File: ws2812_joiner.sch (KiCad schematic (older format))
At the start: 22 parts, among them P1 CONN_01X03, P10 CONN_01X03, P2 CONN_01X03, P3 CONN_01X03, P4 CONN_01X03, P5 CONN_01X03, P6 CONN_01X03, P7 CONN_01X03, P8 CONN_01X03, P9 CONN_01X03

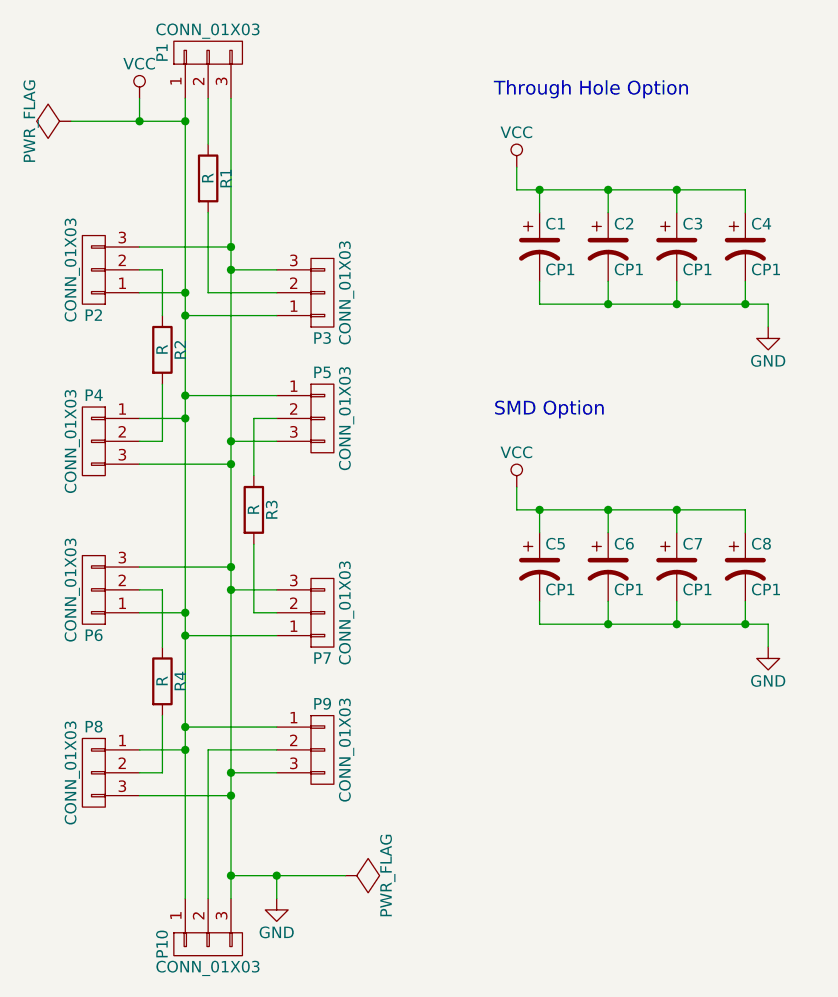
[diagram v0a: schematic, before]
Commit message: Version 2 - use SMD tantalum caps to neaten everything up. Duplicate silkscreen graphics to the front where possible and add component values.
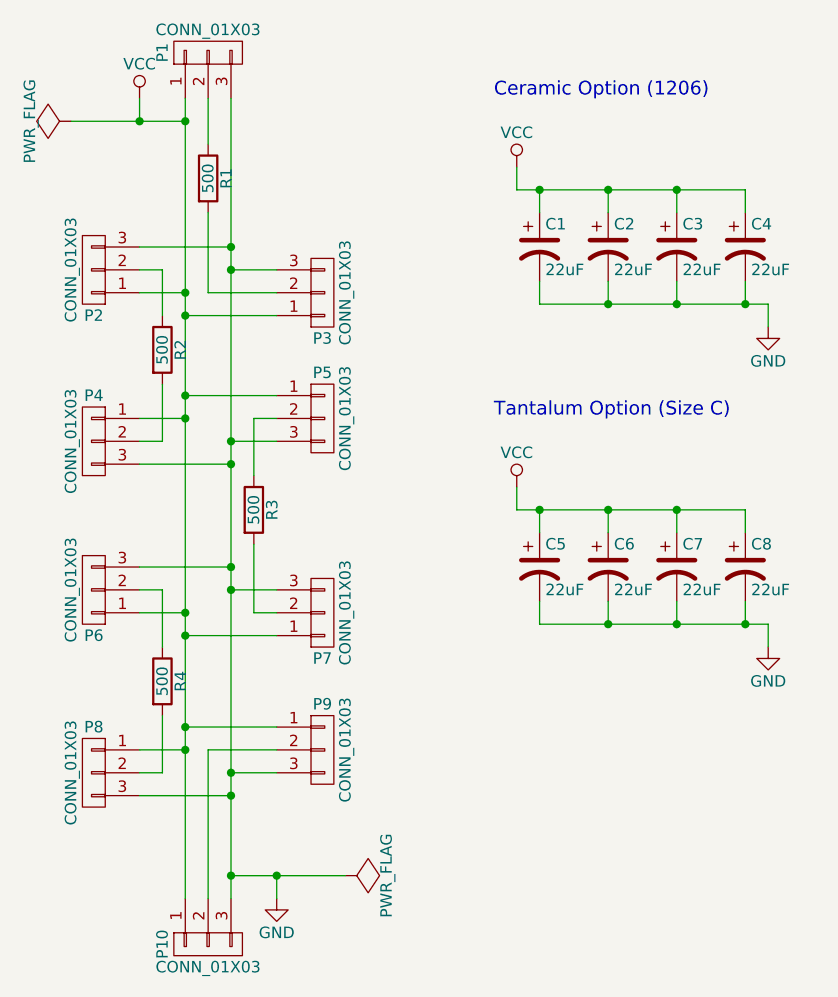
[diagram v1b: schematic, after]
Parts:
- C1, C2, C3, C4: value CP1 -> 22uF; footprint Capacitors_ThroughHole:CP_Radial_D10.0mm_P2.50mm_P5.00mm -> Capacitors_Tantalum_SMD:CP_Tantalum_Case-C_EIA-6032-28_Reflow
- C5, C6, C7, C8: value CP1 -> 22uF
- R1, R2, R3, R4: value R -> 500
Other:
- note added: "Ceramic Option (1206)"
- note added: "Tantalum Option (Size C)"
- note removed: "SMD Option"
- note removed: "Through Hole Option"
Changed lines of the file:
@@
 P 7200 2700
 F 0 "C1" H 7225 2800 50  0000 L CNN
-F 1 "CP1" H 7225 2600 50  0000 L CNN
-F 2 "Capacitors_ThroughHole:CP_Radial_D10.0mm_P2.50mm_P5.00mm" H 7200 2700 50  0001 C CNN
+F 1 "22uF" H 7225 2600 50  0000 L CNN
+F 2 "Capacitors_Tantalum_SMD:CP_Tantalum_Case-C_EIA-6032-28_Reflow" H 7200 2700 50  0001 C CNN
 F 3 "" H 7200 2700 50  0000 C CNN
 	1    7200 2700
@@
 P 7500 2700
 F 0 "C2" H 7525 2800 50  0000 L CNN
-F 1 "CP1" H 7525 2600 50  0000 L CNN
-F 2 "Capacitors_ThroughHole:CP_Radial_D10.0mm_P2.50mm_P5.00mm" H 7500 2700 50  0001 C CNN
+F 1 "22uF" H 7525 2600 50  0000 L CNN
+F 2 "Capacitors_Tantalum_SMD:CP_Tantalum_Case-C_EIA-6032-28_Reflow" H 7500 2700 50  0001 C CNN
 F 3 "" H 7500 2700 50  0000 C CNN
 	1    7500 2700
@@
 P 7800 2700
 F 0 "C3" H 7825 2800 50  0000 L CNN
-F 1 "CP1" H 7825 2600 50  0000 L CNN
-F 2 "Capacitors_ThroughHole:CP_Radial_D10.0mm_P2.50mm_P5.00mm" H 7800 2700 50  0001 C CNN
+F 1 "22uF" H 7825 2600 50  0000 L CNN
+F 2 "Capacitors_Tantalum_SMD:CP_Tantalum_Case-C_EIA-6032-28_Reflow" H 7800 2700 50  0001 C CNN
 F 3 "" H 7800 2700 50  0000 C CNN
 	1    7800 2700
@@
 P 8100 2700
 F 0 "C4" H 8125 2800 50  0000 L CNN
-F 1 "CP1" H 8125 2600 50  0000 L CNN
-F 2 "Capacitors_ThroughHole:CP_Radial_D10.0mm_P2.50mm_P5.00mm" H 8100 2700 50  0001 C CNN
+F 1 "22uF" H 8125 2600 50  0000 L CNN
+F 2 "Capacitors_Tantalum_SMD:CP_Tantalum_Case-C_EIA-6032-28_Reflow" H 8100 2700 50  0001 C CNN
 F 3 "" H 8100 2700 50  0000 C CNN
 	1    8100 2700
@@
 P 5550 3150
 F 0 "R2" V 5630 3150 50  0000 C CNN
-F 1 "R" V 5550 3150 50  0000 C CNN
+F 1 "500" V 5550 3150 50  0000 C CNN
 F 2 "Resistors_SMD:R_1206_HandSoldering" V 5480 3150 50  0001 C CNN
 F 3 "" H 5550 3150 50  0000 C CNN
@@
 P 5950 3850
 F 0 "R3" V 6030 3850 50  0000 C CNN
-F 1 "R" V 5950 3850 50  0000 C CNN
+F 1 "500" V 5950 3850 50  0000 C CNN
 F 2 "Resistors_SMD:R_1206_HandSoldering" V 5880 3850 50  0001 C CNN
 F 3 "" H 5950 3850 50  0000 C CNN
@@
 P 5550 4600
 F 0 "R4" V 5630 4600 50  0000 C CNN
-F 1 "R" V 5550 4600 50  0000 C CNN
+F 1 "500" V 5550 4600 50  0000 C CNN
 F 2 "Resistors_SMD:R_1206_HandSoldering" V 5480 4600 50  0001 C CNN
 F 3 "" H 5550 4600 50  0000 C CNN
@@
 P 5750 2400
 F 0 "R1" V 5830 2400 50  0000 C CNN
-F 1 "R" V 5750 2400 50  0000 C CNN
+F 1 "500" V 5750 2400 50  0000 C CNN
 F 2 "Resistors_SMD:R_1206_HandSoldering" V 5680 2400 50  0001 C CNN
 F 3 "" H 5750 2400 50  0000 C CNN
@@
 P 7200 4100
 F 0 "C5" H 7225 4200 50  0000 L CNN
-F 1 "CP1" H 7225 4000 50  0000 L CNN
+F 1 "22uF" H 7225 4000 50  0000 L CNN
 F 2 "Capacitors_SMD:C_1206_HandSoldering" H 7200 4100 50  0001 C CNN
 F 3 "" H 7200 4100 50  0000 C CNN
@@
 P 7500 4100
 F 0 "C6" H 7525 4200 50  0000 L CNN
-F 1 "CP1" H 7525 4000 50  0000 L CNN
+F 1 "22uF" H 7525 4000 50  0000 L CNN
 F 2 "Capacitors_SMD:C_1206_HandSoldering" H 7500 4100 50  0001 C CNN
 F 3 "" H 7500 4100 50  0000 C CNN
@@
 P 7800 4100
 F 0 "C7" H 7825 4200 50  0000 L CNN
-F 1 "CP1" H 7825 4000 50  0000 L CNN
+F 1 "22uF" H 7825 4000 50  0000 L CNN
 F 2 "Capacitors_SMD:C_1206_HandSoldering" H 7800 4100 50  0001 C CNN
 F 3 "" H 7800 4100 50  0000 C CNN
@@
 P 8100 4100
 F 0 "C8" H 8125 4200 50  0000 L CNN
-F 1 "CP1" H 8125 4000 50  0000 L CNN
+F 1 "22uF" H 8125 4000 50  0000 L CNN
 F 2 "Capacitors_SMD:C_1206_HandSoldering" H 8100 4100 50  0001 C CNN
 F 3 "" H 8100 4100 50  0000 C CNN
@@
 $EndComp
 Text Notes 7000 2050 0    60   ~ 0
-Through Hole Option
+Ceramic Option (1206)
 Text Notes 7000 3450 0    60   ~ 0
-SMD Option
+Tantalum Option (Size C)
 $EndSCHEMATC
